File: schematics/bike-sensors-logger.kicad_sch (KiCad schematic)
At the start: 7 parts, among them J1 MMCX, U1 RaspberryPi_Zero_Dummy

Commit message: Refactor WIP
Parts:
- removed U1: RaspberryPi_Zero_Dummy, RaspberryPiZero_Dummy:RaspberryPiZero_Dummy, symbol Raspberry PI Zero:RaspberryPi_Zero_Dummy
- R5, R6: footprint (none) -> Resistor_SMD:R_0603_1608Metric
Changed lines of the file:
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@@
-	)
-	(symbol
-		(lib_id "Raspberry PI Zero:RaspberryPi_Zero_Dummy")
-		(at 78.74 46.99 0)
-		(unit 1)
-		(exclude_from_sim no)
-		(in_bom yes)
-		(on_board yes)
-		(dnp no)
-		(fields_autoplaced yes)
-		(property "Reference" "U1"
-			(at 80.01 45.7199 0)
-			(effects
-				(font
-					(size 1.27 1.27)
-				)
-				(justify left)
-				(hide yes)
-			)
-		)
-		(property "Value" "RaspberryPi_Zero_Dummy"
-			(at 80.01 48.2599 0)
-			(effects
-				(font
-					(size 1.27 1.27)
-				)
-				(justify left)
-				(hide yes)
-			)
-		)
-		(property "Footprint" "RaspberryPiZero_Dummy:RaspberryPiZero_Dummy"
-			(at 78.74 46.99 0)
-			(effects
-				(font
-					(size 1.27 1.27)
-				)
-				(hide yes)
-			)
-		)
-		(property "Datasheet" ""
-			(at 78.74 46.99 0)
-			(effects
-				(font
-					(size 1.27 1.27)
-				)
-				(hide yes)
-			)
-		)
-		(property "Description" ""
-			(at 78.74 46.99 0)
-			(effects
-				(font
-					(size 1.27 1.27)
-				)
-				(hide yes)
-			)
-		)
-		(instances
-			(project ""
-				(path "/2c1d9222-af16-428b-85a5-a3d420373d70"
-					(reference "U1")
-					(unit 1)
-				)
-			)
-		)
 	)
 	(symbol
@@
 			)
 		)
-		(property "Footprint" ""
+		(property "Footprint" "Resistor_SMD:R_0603_1608Metric"
 			(at 88.9 113.538 90)
 			(effects
@@
 			)
 		)
-		(property "Footprint" ""
+		(property "Footprint" "Resistor_SMD:R_0603_1608Metric"
 			(at 88.9 97.028 90)
 			(effects

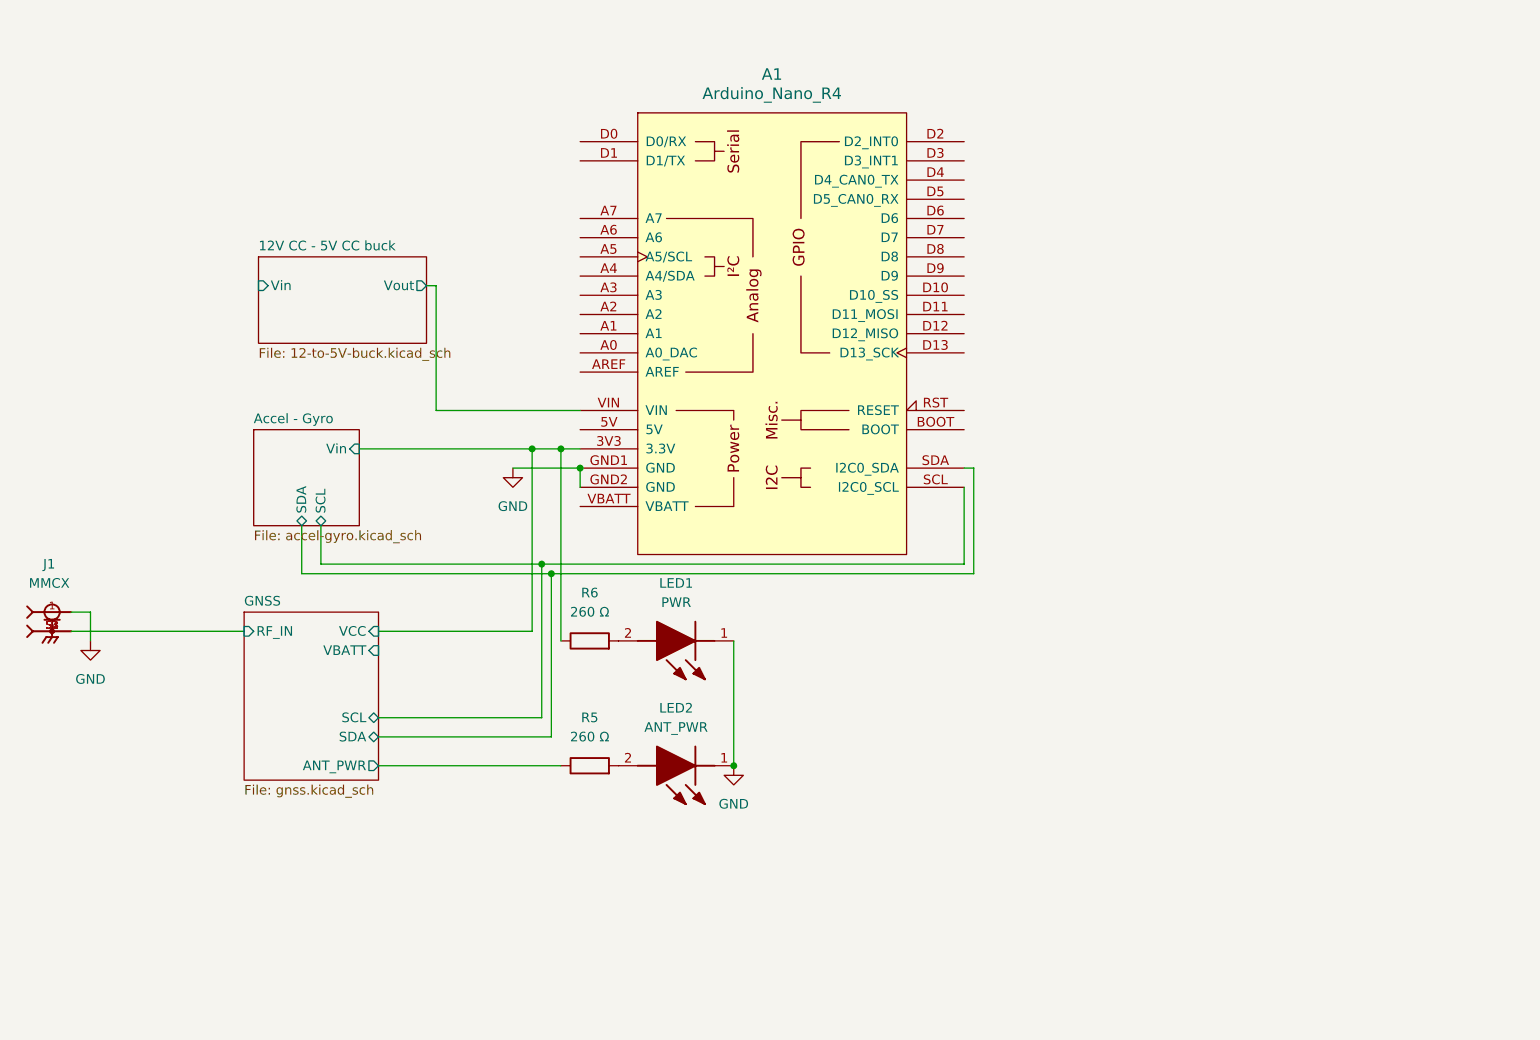
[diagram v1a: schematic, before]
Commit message: Added OBD II connection + OBD II termination check; library scaffolding refactor
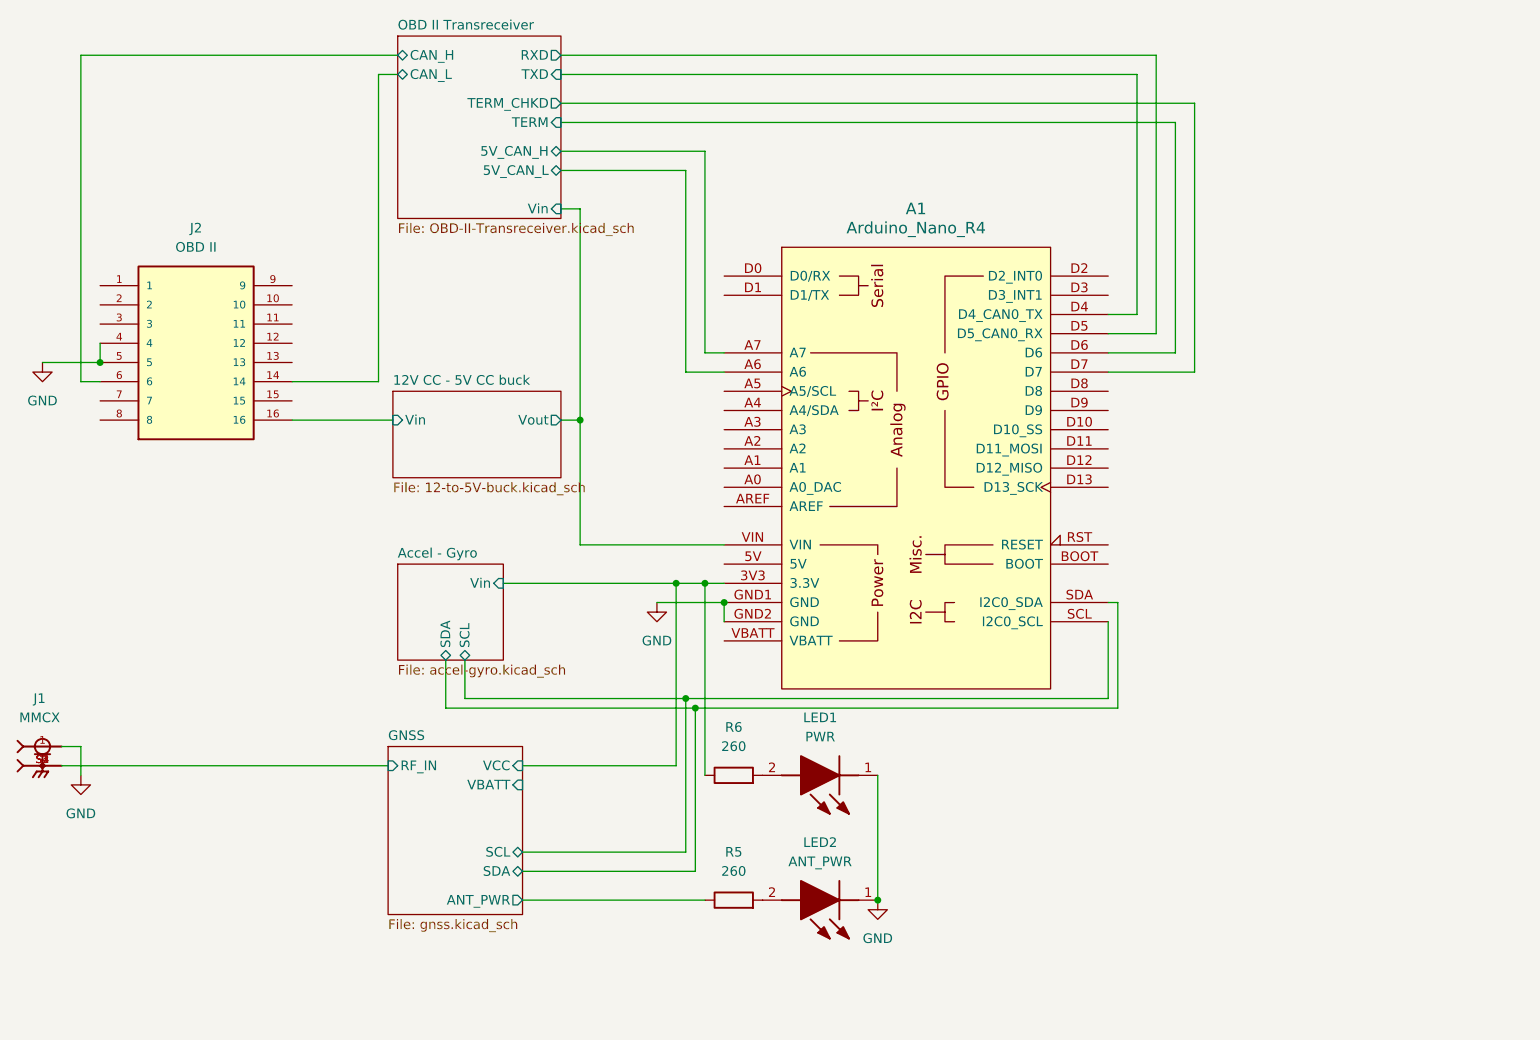
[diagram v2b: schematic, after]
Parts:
- added J2: OBD II, C-OBD-II-16M:COMTECH_C-OBD-II-16M, symbol C-OBD-II-16M:C-OBD-II-16M
- R5, R6: value 260 Ω -> 260
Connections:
- net 12V CC - 5V CC buck/Vin: now also J2.16
- net GND: now also J2.4, J2.5
- net OBD II Transreceiver/5V_CAN_L: now reaches A1.A6
- net OBD II Transreceiver/5V_CAN_H: now reaches A1.A7
- net OBD II Transreceiver/TXD: now reaches A1.D4 (D4_CAN0_TX)
- net OBD II Transreceiver/RXD: now reaches A1.D5 (D5_CAN0_RX)
- net OBD II Transreceiver/TERM: now reaches A1.D6
- net OBD II Transreceiver/TERM_CHKD: now reaches A1.D7
- new net OBD II Transreceiver/CAN_H: J2.6
- new net OBD II Transreceiver/CAN_L: J2.14
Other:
- added sheet OBD II Transreceiver (OBD-II-Transreceiver.kicad_sch)
- moved on the sheet: A1, J1, LED1, LED2, R5, R6

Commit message: OBD II clamping schematic simplification; README file update. Small repositionings.
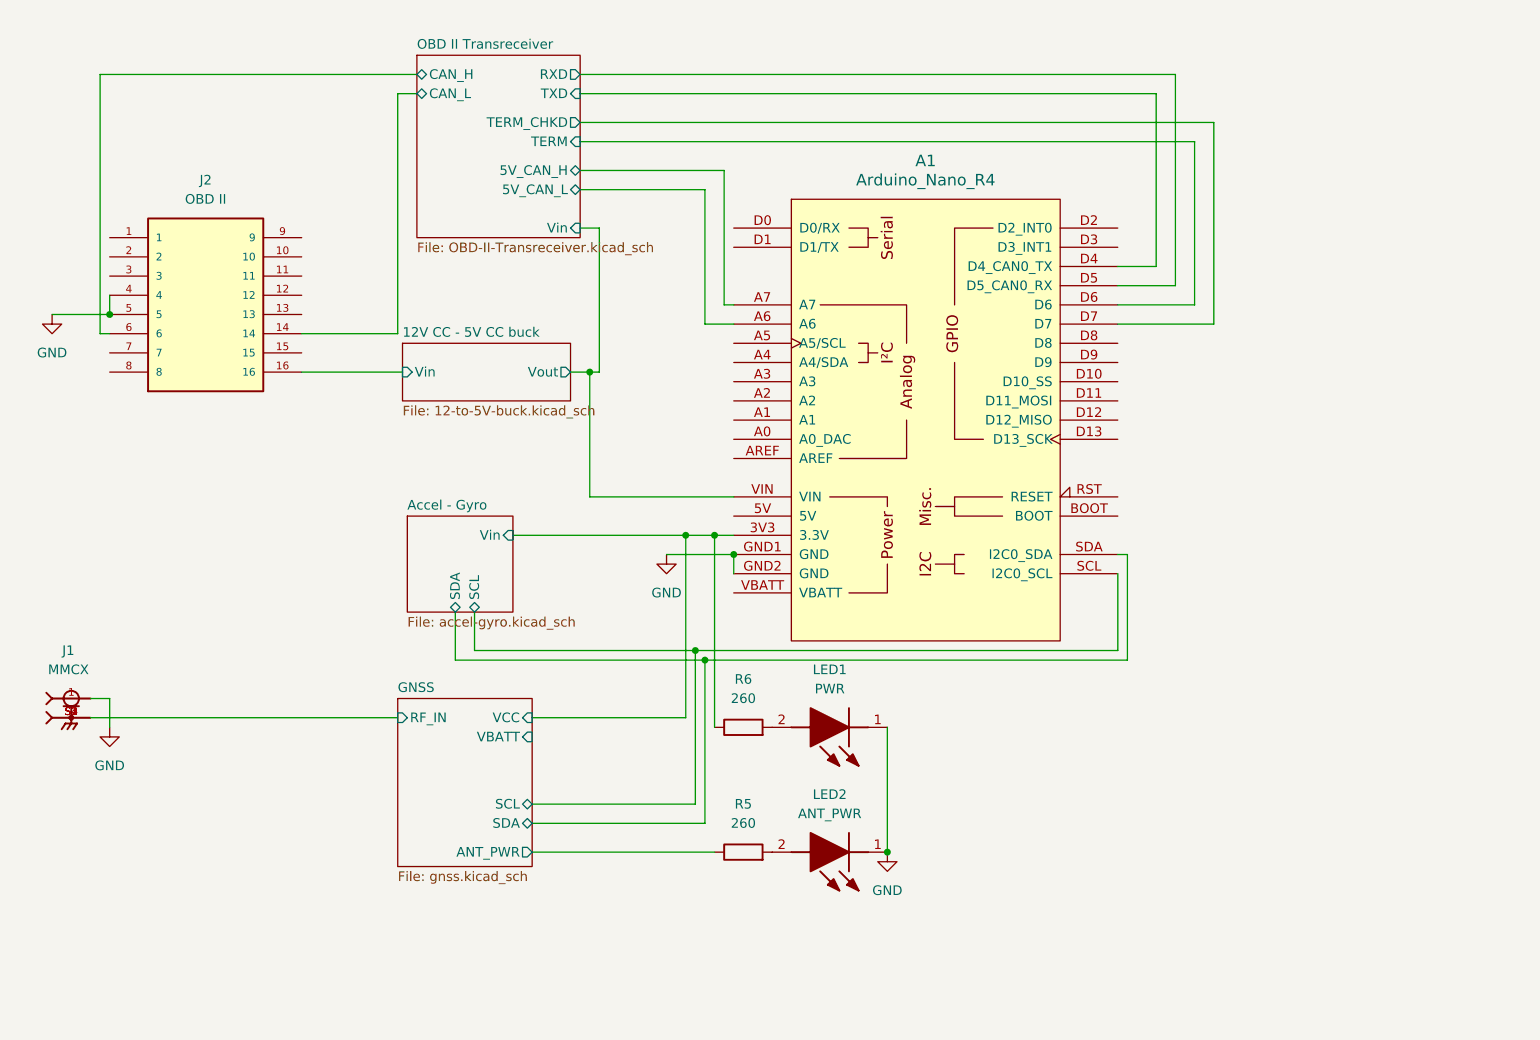
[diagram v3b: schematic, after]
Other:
- moved on the sheet: A1, J1, J2, LED1, LED2, R5, R6

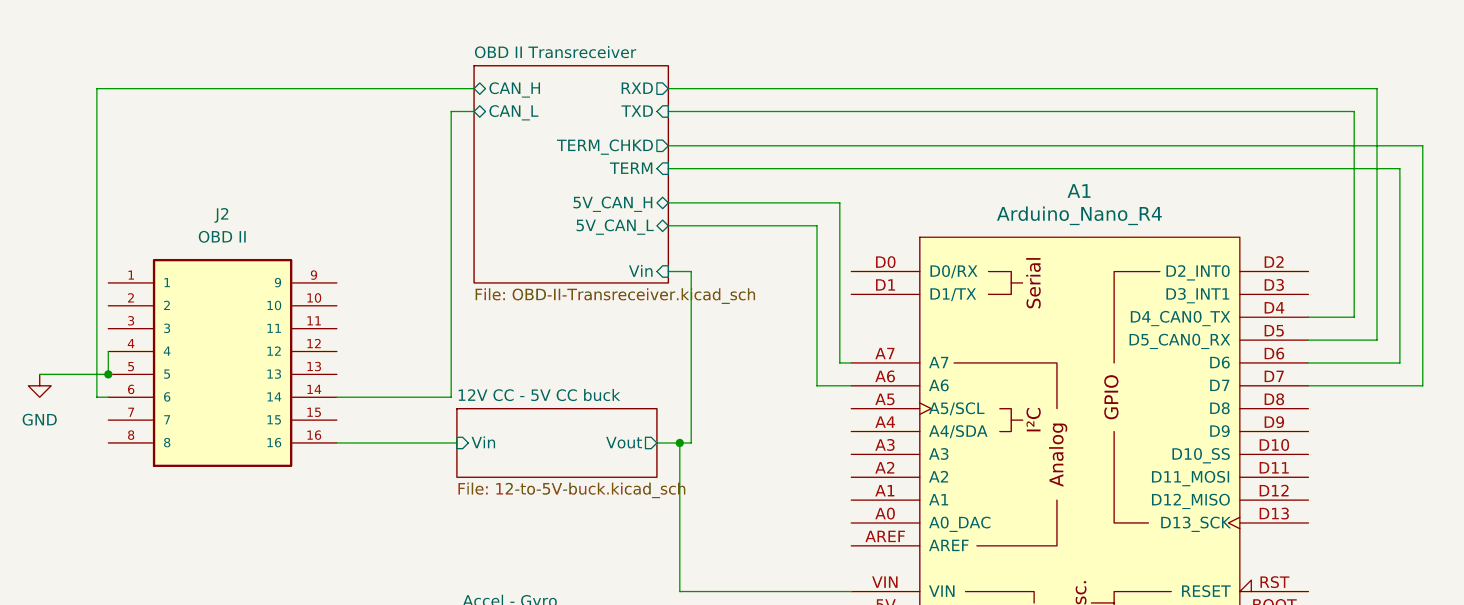
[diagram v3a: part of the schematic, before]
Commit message: Fixed OBD II termination check (schem + firm)
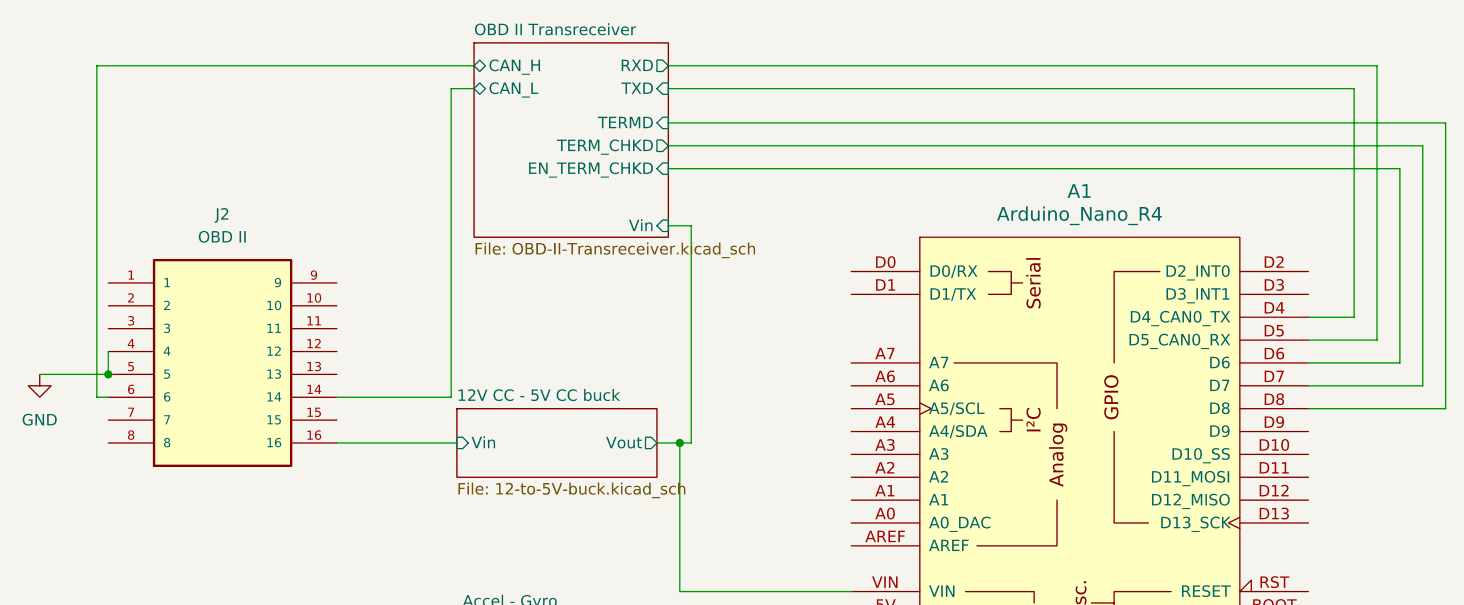
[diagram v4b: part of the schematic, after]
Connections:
- net OBD II Transreceiver/TERMD: now reaches A1.D8
- net OBD II Transreceiver/5V_CAN_H: no longer names the net of A1.A7
- net OBD II Transreceiver/5V_CAN_L: no longer names the net of A1.A6
- net OBD II Transreceiver/TERM renamed OBD II Transreceiver/EN_TERM_CHKD
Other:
- sheet OBD II Transreceiver ports: added EN_TERM_CHKD, TERMD; removed 5V_CAN_H, 5V_CAN_L, TERM
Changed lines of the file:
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@@
 	(wire
 		(pts
-			(xy 90.17 40.64) (xy 90.17 59.69)
+			(xy 90.17 35.56) (xy 90.17 59.69)
 		)
 		(stroke
@@
 	(wire
 		(pts
+			(xy 171.45 26.67) (xy 171.45 53.34)
+		)
+		(stroke
+			(width 0)
+			(type default)
+		)
+	)
+	(wire
+		(pts
 			(xy 81.28 123.19) (xy 105.41 123.19)
 		)
@@
 	(wire
 		(pts
-			(xy 87.63 33.02) (xy 106.68 33.02)
-		)
-		(stroke
-			(width 0)
-			(type default)
-		)
-	)
-	(wire
-		(pts
-			(xy 163.83 22.86) (xy 163.83 45.72)
+			(xy 163.83 20.32) (xy 163.83 45.72)
 		)
 		(stroke
@@
 	(wire
 		(pts
-			(xy 24.13 20.32) (xy 66.04 20.32)
+			(xy 24.13 17.78) (xy 66.04 17.78)
 		)
 		(stroke
@@
 	(wire
 		(pts
-			(xy 168.91 29.21) (xy 168.91 50.8)
-		)
-		(stroke
-			(width 0)
-			(type default)
-		)
-	)
-	(wire
-		(pts
 			(xy 158.75 48.26) (xy 166.37 48.26)
 		)
@@
 	(wire
 		(pts
-			(xy 104.14 53.34) (xy 107.95 53.34)
-		)
-		(stroke
-			(width 0)
-			(type default)
-		)
-	)
-	(wire
-		(pts
 			(xy 78.74 81.28) (xy 101.6 81.28)
 		)
@@
 	(wire
 		(pts
-			(xy 87.63 35.56) (xy 104.14 35.56)
-		)
-		(stroke
-			(width 0)
-			(type default)
-		)
-	)
-	(wire
-		(pts
 			(xy 71.12 91.44) (xy 71.12 97.79)
 		)
@@
 	(wire
 		(pts
-			(xy 171.45 26.67) (xy 171.45 53.34)
-		)
-		(stroke
-			(width 0)
-			(type default)
-		)
-	)
-	(wire
-		(pts
-			(xy 87.63 22.86) (xy 163.83 22.86)
-		)
-		(stroke
-			(width 0)
-			(type default)
-		)
-	)
-	(wire
-		(pts
-			(xy 63.5 22.86) (xy 66.04 22.86)
+			(xy 87.63 20.32) (xy 163.83 20.32)
+		)
+		(stroke
+			(width 0)
+			(type default)
+		)
+	)
+	(wire
+		(pts
+			(xy 63.5 20.32) (xy 66.04 20.32)
 		)
 		(stroke
@@
 	(wire
 		(pts
+			(xy 87.63 26.67) (xy 171.45 26.67)
+		)
+		(stroke
+			(width 0)
+			(type default)
+		)
+	)
+	(wire
+		(pts
+			(xy 166.37 17.78) (xy 166.37 48.26)
+		)
+		(stroke
+			(width 0)
+			(type default)
+		)
+	)
+	(wire
+		(pts
+			(xy 17.78 52.07) (xy 25.4 52.07)
+		)
+		(stroke
+			(width 0)
+			(type default)
+		)
+	)
+	(wire
+		(pts
+			(xy 81.28 119.38) (xy 104.14 119.38)
+		)
+		(stroke
+			(width 0)
+			(type default)
+		)
+	)
+	(wire
+		(pts
+			(xy 168.91 50.8) (xy 168.91 29.21)
+		)
+		(stroke
+			(width 0)
+			(type default)
+		)
+	)
+	(wire
+		(pts
+			(xy 87.63 35.56) (xy 90.17 35.56)
+		)
+		(stroke
+			(width 0)
+			(type default)
+		)
+	)
+	(wire
+		(pts
+			(xy 87.63 17.78) (xy 166.37 17.78)
+		)
+		(stroke
+			(width 0)
+			(type default)
+		)
+	)
+	(wire
+		(pts
+			(xy 160.02 97.79) (xy 160.02 83.82)
+		)
+		(stroke
+			(width 0)
+			(type default)
+		)
+	)
+	(wire
+		(pts
+			(xy 158.75 53.34) (xy 171.45 53.34)
+		)
+		(stroke
+			(width 0)
+			(type default)
+		)
+	)
+	(wire
+		(pts
+			(xy 158.75 50.8) (xy 168.91 50.8)
+		)
+		(stroke
+			(width 0)
+			(type default)
+		)
+	)
+	(wire
+		(pts
 			(xy 87.63 29.21) (xy 168.91 29.21)
 		)
@@
 	(wire
 		(pts
-			(xy 166.37 20.32) (xy 166.37 48.26)
-		)
-		(stroke
-			(width 0)
-			(type default)
-		)
-	)
-	(wire
-		(pts
-			(xy 17.78 52.07) (xy 25.4 52.07)
-		)
-		(stroke
-			(width 0)
-			(type default)
-		)
-	)
-	(wire
-		(pts
-			(xy 81.28 119.38) (xy 104.14 119.38)
-		)
-		(stroke
-			(width 0)
-			(type default)
-		)
-	)
-	(wire
-		(pts
-			(xy 87.63 40.64) (xy 90.17 40.64)
-		)
-		(stroke
-			(width 0)
-			(type default)
-		)
-	)
-	(wire
-		(pts
-			(xy 87.63 20.32) (xy 166.37 20.32)
-		)
-		(stroke
-			(width 0)
-			(type default)
-		)
-	)
-	(wire
-		(pts
-			(xy 160.02 97.79) (xy 160.02 83.82)
-		)
-		(stroke
-			(width 0)
-			(type default)
-		)
-	)
-	(wire
-		(pts
-			(xy 106.68 33.02) (xy 106.68 50.8)
-		)
-		(stroke
-			(width 0)
-			(type default)
-		)
-	)
-	(wire
-		(pts
-			(xy 158.75 53.34) (xy 171.45 53.34)
-		)
-		(stroke
-			(width 0)
-			(type default)
-		)
-	)
-	(wire
-		(pts
-			(xy 158.75 50.8) (xy 168.91 50.8)
-		)
-		(stroke
-			(width 0)
-			(type default)
-		)
-	)
-	(wire
-		(pts
 			(xy 128.27 106.68) (xy 128.27 123.19)
 		)
@@
 	(wire
 		(pts
+			(xy 158.75 55.88) (xy 173.99 55.88)
+		)
+		(stroke
+			(width 0)
+			(type default)
+		)
+	)
+	(wire
+		(pts
 			(xy 50.8 59.69) (xy 64.135 59.69)
 		)
@@
 	(wire
 		(pts
-			(xy 87.63 26.67) (xy 171.45 26.67)
+			(xy 173.99 24.13) (xy 173.99 55.88)
 		)
 		(stroke
@@
 	(wire
 		(pts
-			(xy 106.68 50.8) (xy 107.95 50.8)
+			(xy 87.63 24.13) (xy 173.99 24.13)
 		)
 		(stroke
@@
 	(wire
 		(pts
-			(xy 24.13 54.61) (xy 24.13 20.32)
-		)
-		(stroke
-			(width 0)
-			(type default)
-		)
-	)
-	(wire
-		(pts
-			(xy 104.14 35.56) (xy 104.14 53.34)
+			(xy 24.13 54.61) (xy 24.13 17.78)
 		)
 		(stroke
@@
 	(wire
 		(pts
-			(xy 63.5 54.61) (xy 63.5 22.86)
+			(xy 63.5 54.61) (xy 63.5 20.32)
 		)
 		(stroke
@@
 	)
 	(sheet
-		(at 66.04 17.78)
-		(size 21.59 24.13)
+		(at 66.04 15.24)
+		(size 21.59 21.59)
 		(exclude_from_sim no)
 		(in_bom yes)
@@
 		)
 		(property "Sheetname" "OBD II Transreceiver"
-			(at 66.04 17.0684 0)
+			(at 66.04 14.5284 0)
 			(effects
 				(font
@@
 		)
 		(property "Sheetfile" "OBD-II-Transreceiver.kicad_sch"
-			(at 66.04 42.4946 0)
+			(at 66.04 37.4146 0)
 			(effects
 				(font
@@
 		)
 		(pin "CAN_H" bidirectional
+			(at 66.04 17.78 180)
+			(effects
+				(font
+					(size 1.27 1.27)
+				)
+				(justify left)
+			)
+		)
+		(pin "CAN_L" bidirectional
 			(at 66.04 20.32 180)
 			(effects
@@
 			)
 		)
-		(pin "CAN_L" bidirectional
-			(at 66.04 22.86 180)
-			(effects
-				(font
-					(size 1.27 1.27)
-				)
-				(justify left)
-			)
-		)
 		(pin "RXD" output
-			(at 87.63 20.32 0)
+			(at 87.63 17.78 0)
 			(effects
 				(font
@@
 			)
 		)
-		(pin "TERM" input
-			(at 87.63 29.21 0)
+		(pin "TERMD" input
+			(at 87.63 24.13 0)
 			(effects
 				(font
@@
 		)
 		(pin "TXD" input
-			(at 87.63 22.86 0)
+			(at 87.63 20.32 0)
 			(effects
 				(font
@@
 		)
 		(pin "Vin" input
-			(at 87.63 40.64 0)
+			(at 87.63 35.56 0)
 			(effects
 				(font
@@
 			)
 		)
-		(pin "5V_CAN_H" bidirectional
-			(at 87.63 33.02 0)
-			(effects
-				(font
-					(size 1.27 1.27)
-				)
-				(justify right)
-			)
-		)
-		(pin "5V_CAN_L" bidirectional
-			(at 87.63 35.56 0)
-			(effects
-				(font
+		(pin "EN_TERM_CHKD" input
+			(at 87.63 29.21 0)
+			(effects
+				(font
